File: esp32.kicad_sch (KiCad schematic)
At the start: 37 parts, among them J1 104426-8, J2 104426-8, SW1 SW_Push, SW2 SW_Push, SW3 SW_Push, SW4 SW_Push, U5 ESP32-WROOM-32D

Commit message: Organização do sheet esp32
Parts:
- renumbered C29 to C28, C30 to C29, C28 to C30
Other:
- moved on the sheet: C28, C29, J1, J2, R37, R38, R39, R40, R41, R42, R43, R44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

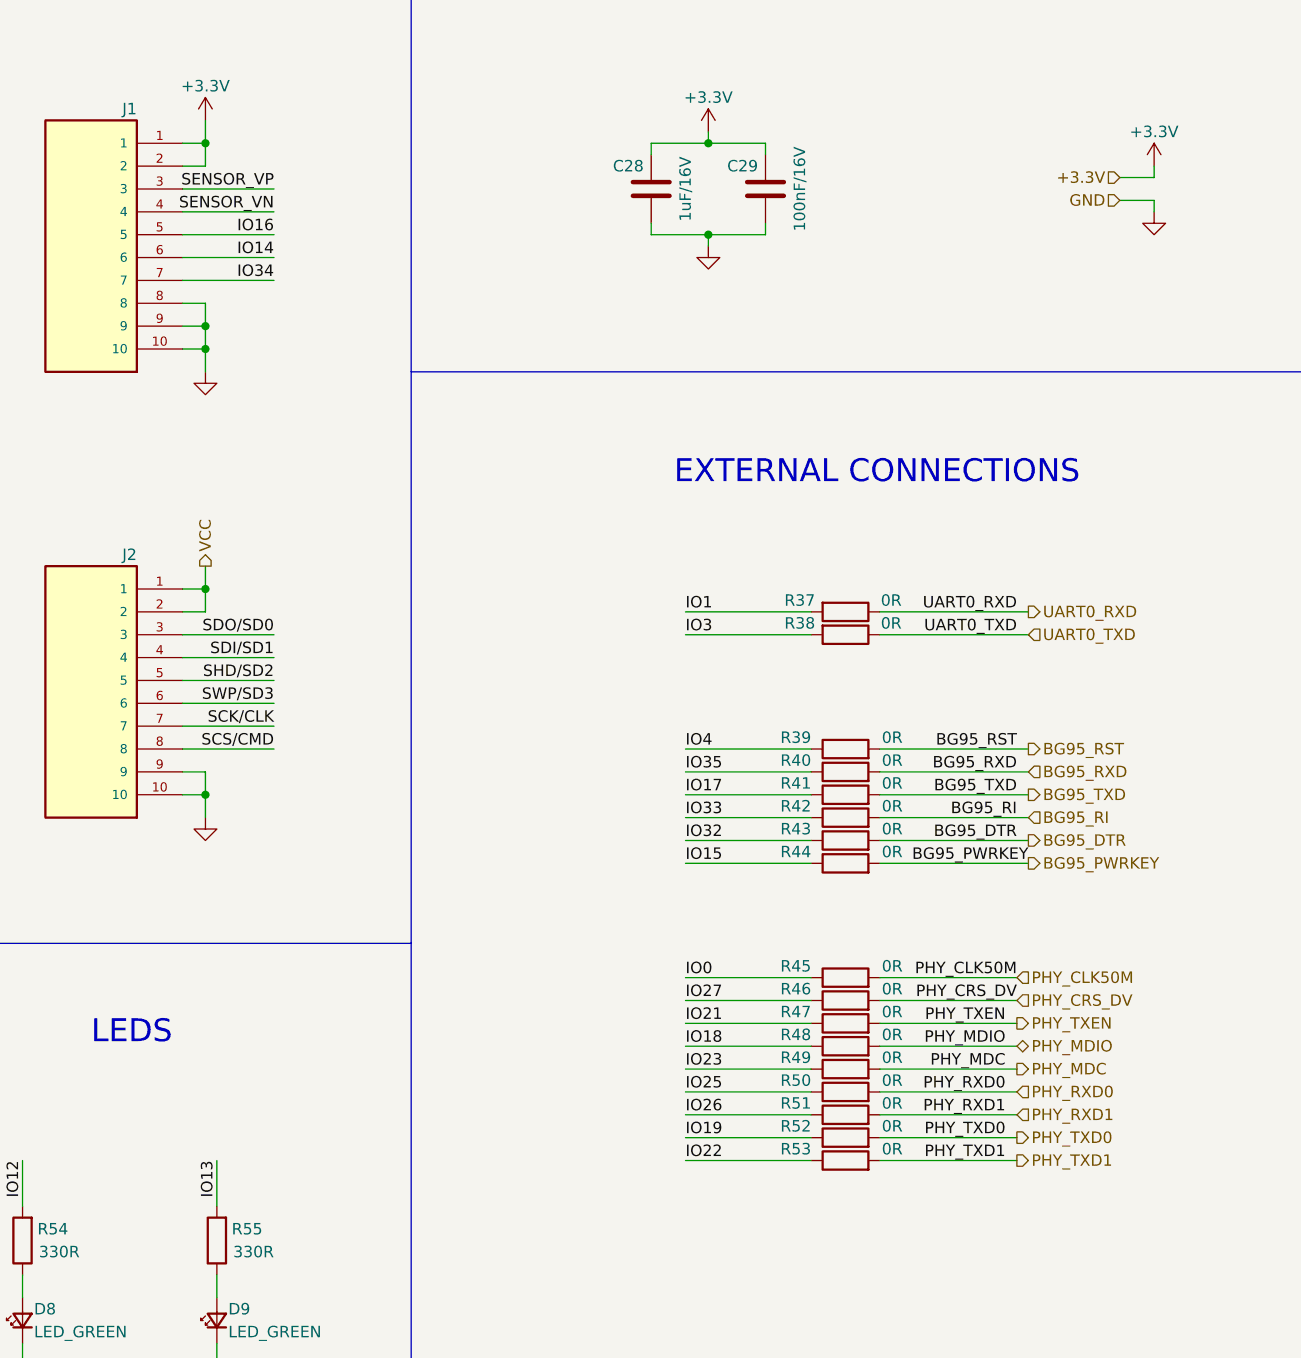
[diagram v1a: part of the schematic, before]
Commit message: Inserido um pino de controle de reset do PHY
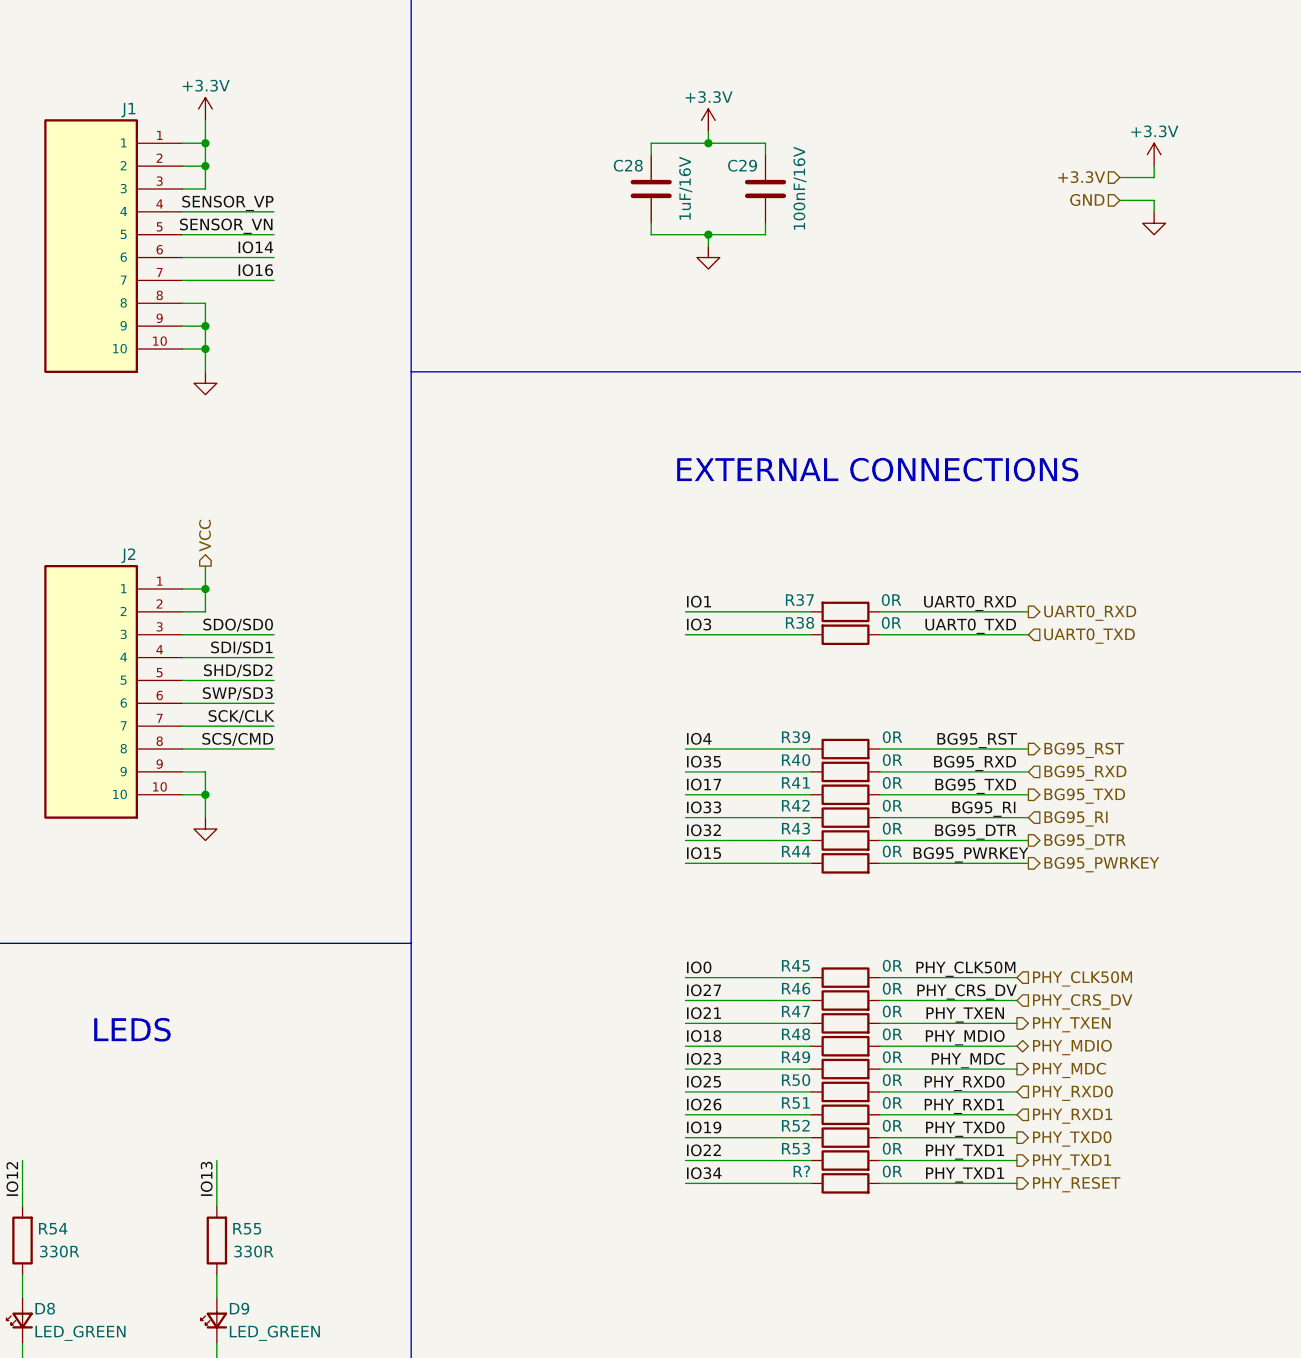
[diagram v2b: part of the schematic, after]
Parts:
- added R?: 0R, Resistor_SMD:R_0603_1608Metric_Pad0.98x0.95mm_HandSolder, symbol Device:R
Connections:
- net +3V3: now also J1.3
- net IO16: now also J1.7; no longer J1.5
- net IO34: now also R?.1; no longer J1.7
- net SENSOR_VN: now also J1.5; no longer J1.4
- net SENSOR_VP: now also J1.4; no longer J1.3
- net PHY_TXD1 renamed PHY_RESET
- net PHY_RESET: now also R?.2
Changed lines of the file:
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@@
   (junction (at 153.67 111.76) (diameter 0) (color 0 0 0 0)
   )
+  (junction (at 153.67 41.91) (diameter 0) (color 0 0 0 0)
+  )
   (junction (at 209.55 39.37) (diameter 0) (color 0 0 0 0)
   )
@@
     (stroke (width 0) (type default) (color 0 0 0 0))
   )
+  (wire (pts (xy 151.13 54.61) (xy 161.29 54.61))
+    (stroke (width 0) (type default) (color 0 0 0 0))
+  )
   (wire (pts (xy 220.98 91.44) (xy 207.01 91.44))
     (stroke (width 0) (type default) (color 0 0 0 0))
@@
     (stroke (width 0) (type default) (color 0 0 0 0))
   )
+  (wire (pts (xy 207.01 154.94) (xy 220.98 154.94))
+    (stroke (width 0) (type default) (color 0 0 0 0))
+  )
   (wire (pts (xy 228.6 137.16) (xy 243.84 137.16))
     (stroke (width 0) (type default) (color 0 0 0 0))
@@
     (stroke (width 0) (type default) (color 0 0 0 0))
   )
+  (wire (pts (xy 228.6 154.94) (xy 243.84 154.94))
+    (stroke (width 0) (type default) (color 0 0 0 0))
+  )
   (wire (pts (xy 90.17 96.52) (xy 99.06 96.52))
     (stroke (width 0) (type default) (color 0 0 0 0))
@@
     (stroke (width 0) (type default) (color 0 0 0 0))
   )
+  (wire (pts (xy 153.67 44.45) (xy 153.67 41.91))
+    (stroke (width 0) (type default) (color 0 0 0 0))
+  )
   (wire (pts (xy 228.6 111.76) (xy 245.11 111.76))
     (stroke (width 0) (type default) (color 0 0 0 0))
@@
     (stroke (width 0) (type default) (color 0 0 0 0))
   )
-  (wire (pts (xy 151.13 54.61) (xy 161.29 54.61))
-    (stroke (width 0) (type default) (color 0 0 0 0))
-  )
   (wire (pts (xy 215.9 48.26) (xy 215.9 49.53))
     (stroke (width 0) (type default) (color 0 0 0 0))
@@
     (stroke (width 0) (type default) (color 0 0 0 0))
   )
-  (wire (pts (xy 151.13 44.45) (xy 161.29 44.45))
-    (stroke (width 0) (type default) (color 0 0 0 0))
-  )
   (wire (pts (xy 153.67 36.83) (xy 153.67 39.37))
     (stroke (width 0) (type default) (color 0 0 0 0))
@@
   )
   (wire (pts (xy 228.6 91.44) (xy 245.11 91.44))
+    (stroke (width 0) (type default) (color 0 0 0 0))
+  )
+  (wire (pts (xy 151.13 44.45) (xy 153.67 44.45))
     (stroke (width 0) (type default) (color 0 0 0 0))
   )
@@
     (effects (font (size 1.27 1.27)) (justify left bottom))
   )
-  (label "IO16" (at 161.29 49.53 180)
+  (label "SENSOR_VN" (at 161.29 49.53 180)
     (effects (font (size 1.27 1.27)) (justify right bottom))
   )
@@
     (effects (font (size 1.27 1.27)) (justify left bottom))
   )
+  (label "PHY_TXD1" (at 242.57 154.94 180)
+    (effects (font (size 1.27 1.27)) (justify right bottom))
+  )
   (label "PHY_TXD0" (at 242.57 149.86 180)
     (effects (font (size 1.27 1.27)) (justify right bottom))
@@
     (effects (font (size 1.27 1.27)) (justify left bottom))
   )
-  (label "SENSOR_VN" (at 161.29 46.99 180)
+  (label "SENSOR_VP" (at 161.29 46.99 180)
     (effects (font (size 1.27 1.27)) (justify right bottom))
   )
@@
     (effects (font (size 1.27 1.27)) (justify right bottom))
   )
-  (label "IO34" (at 161.29 54.61 180)
-    (effects (font (size 1.27 1.27)) (justify right bottom))
+  (label "IO34" (at 207.01 154.94 0)
+    (effects (font (size 1.27 1.27)) (justify left bottom))
   )
   (label "IO32" (at 207.01 116.84 0)
@@
     (effects (font (size 1.27 1.27)) (justify left bottom))
   )
-  (label "SENSOR_VP" (at 161.29 44.45 180)
-    (effects (font (size 1.27 1.27)) (justify right bottom))
-  )
   (label "SENSOR_VP" (at 48.26 50.8 0)
     (effects (font (size 1.27 1.27)) (justify left bottom))
@@
   )
   (label "IO1" (at 99.06 48.26 180)
+    (effects (font (size 1.27 1.27)) (justify right bottom))
+  )
+  (label "IO16" (at 161.29 54.61 180)
     (effects (font (size 1.27 1.27)) (justify right bottom))
   )
@@
   )
   (hierarchical_label "PHY_CRS_DV" (shape input) (at 243.84 134.62 0)
+    (effects (font (size 1.27 1.27)) (justify left))
+  )
+  (hierarchical_label "PHY_RESET" (shape output) (at 243.84 154.94 0)
     (effects (font (size 1.27 1.27)) (justify left))
   )
@@
     (pin "9")
   )
+  (symbol (lib_id "Device:R") (at 224.79 154.94 90) (unit 1)
+    (in_bom yes) (on_board yes)
+    (property "Reference" "R?" (id 0) (at 220.98 153.67 90)
+      (effects (font (size 1.27 1.27)) (justify left))
+    )
+    (property "Value" "0R" (id 1) (at 231.14 153.67 90)
+      (effects (font (size 1.27 1.27)) (justify left))
+    )
+    (property "Footprint" "Resistor_SMD:R_0603_1608Metric_Pad0.98x0.95mm_HandSolder" (id 2) (at 224.79 156.718 90)
+      (effects (font (size 1.27 1.27)) hide)
+    )
+    (property "Datasheet" "~" (id 3) (at 224.79 154.94 0)
+      (effects (font (size 1.27 1.27)) hide)
+    )
+    (pin "1")
+    (pin "2")
+  )
   (symbol (lib_id "Device:R") (at 224.79 132.08 90) (unit 1)

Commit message: Referencia dos componentes
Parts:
- gave numbers to parts that had none: 1
- renumbered R36 to R37, R37 to R38, R38 to R39, R39 to R40, R40 to R41, R41 to R42, R42 to R43, R43 to R44, R44 to R45, R45 to R46, R46 to R47, R47 to R48, R48 to R49, R49 to R50, R50 to R51, R51 to R52, R52 to R53, R53 to R54, R54 to R56, R55 to R57, R56 to R58, R57 to R59

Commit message: Capacitores com encapsulamento 0603
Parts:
- C28: value 1uF/16V -> (none); footprint Capacitor_SMD:C_0603_1608Metric_Pad1.08x0.95mm_HandSolder -> (none)
- C29, C30, C31, C32, C33: value 100nF/16V -> (none); footprint Capacitor_SMD:C_0402_1005Metric_Pad0.74x0.62mm_HandSolder -> (none)
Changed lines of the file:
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@@
     (in_bom yes) (on_board yes)
     (property "Reference" "C28" (id 0) (at 200.66 41.91 0))
-    (property "Value" "1uF/16V" (id 1) (at 207.01 44.45 90))
-    (property "Footprint" "Capacitor_SMD:C_0603_1608Metric_Pad1.08x0.95mm_HandSolder" (id 2) (at 202.2348 40.64 0)
+    (property "Value" "" (id 1) (at 207.01 44.45 90))
+    (property "Footprint" "" (id 2) (at 202.2348 40.64 0)
       (effects (font (size 1.27 1.27)) hide)
     )
@@
     (in_bom yes) (on_board yes)
     (property "Reference" "C32" (id 0) (at 73.66 171.45 90))
-    (property "Value" "100nF/16V" (id 1) (at 73.66 179.07 90))
-    (property "Footprint" "Capacitor_SMD:C_0402_1005Metric_Pad0.74x0.62mm_HandSolder" (id 2) (at 69.85 176.2252 0)
+    (property "Value" "" (id 1) (at 73.66 179.07 90))
+    (property "Footprint" "" (id 2) (at 69.85 176.2252 0)
       (effects (font (size 1.27 1.27)) hide)
     )
@@
     (in_bom yes) (on_board yes)
     (property "Reference" "C31" (id 0) (at 45.72 171.45 90))
-    (property "Value" "100nF/16V" (id 1) (at 45.72 179.07 90))
-    (property "Footprint" "Capacitor_SMD:C_0402_1005Metric_Pad0.74x0.62mm_HandSolder" (id 2) (at 41.91 176.2252 0)
+    (property "Value" "" (id 1) (at 45.72 179.07 90))
+    (property "Footprint" "" (id 2) (at 41.91 176.2252 0)
       (effects (font (size 1.27 1.27)) hide)
     )
@@
     (in_bom yes) (on_board yes)
     (property "Reference" "C29" (id 0) (at 213.36 41.91 0))
-    (property "Value" "100nF/16V" (id 1) (at 219.71 44.45 90))
-    (property "Footprint" "Capacitor_SMD:C_0402_1005Metric_Pad0.74x0.62mm_HandSolder" (id 2) (at 214.9348 40.64 0)
+    (property "Value" "" (id 1) (at 219.71 44.45 90))
+    (property "Footprint" "" (id 2) (at 214.9348 40.64 0)
       (effects (font (size 1.27 1.27)) hide)
     )
@@
     (in_bom yes) (on_board yes)
     (property "Reference" "C33" (id 0) (at 101.6 171.45 90))
-    (property "Value" "100nF/16V" (id 1) (at 101.6 179.07 90))
-    (property "Footprint" "Capacitor_SMD:C_0402_1005Metric_Pad0.74x0.62mm_HandSolder" (id 2) (at 97.79 176.2252 0)
+    (property "Value" "" (id 1) (at 101.6 179.07 90))
+    (property "Footprint" "" (id 2) (at 97.79 176.2252 0)
       (effects (font (size 1.27 1.27)) hide)
     )
@@
     (in_bom yes) (on_board yes)
     (property "Reference" "C30" (id 0) (at 38.4551 48.5962 0))
-    (property "Value" "100nF/16V" (id 1) (at 44.3458 51.6899 90))
-    (property "Footprint" "Capacitor_SMD:C_0402_1005Metric_Pad0.74x0.62mm_HandSolder" (id 2) (at 39.6748 46.99 0)
-      (effects (font (size 1.27 1.27)) hide)
-    )
+    (property "Value" "" (id 1) (at 44.3458 51.6899 90))
+    (property "Footprint" "" (id 2) (at 39.6748 46.99 0)
+      (effects (font (size 1.27 1.27)) hide)
+    )

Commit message: Adicionado os pads dos Test Point e alterado o Bead
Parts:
- C28: value (none) -> 1uF/16V; footprint (none) -> Capacitor_SMD:C_0603_1608Metric_Pad1.08x0.95mm_HandSolder
- C29, C30, C31, C32, C33: value (none) -> 100nF/16V; footprint (none) -> Capacitor_SMD:C_0603_1608Metric_Pad1.08x0.95mm_HandSolder
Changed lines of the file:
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@@
     (in_bom yes) (on_board yes)
     (property "Reference" "C28" (id 0) (at 200.66 41.91 0))
-    (property "Value" "" (id 1) (at 207.01 44.45 90))
-    (property "Footprint" "" (id 2) (at 202.2348 40.64 0)
+    (property "Value" "1uF/16V" (id 1) (at 207.01 44.45 90))
+    (property "Footprint" "Capacitor_SMD:C_0603_1608Metric_Pad1.08x0.95mm_HandSolder" (id 2) (at 202.2348 40.64 0)
       (effects (font (size 1.27 1.27)) hide)
     )
@@
     (in_bom yes) (on_board yes)
     (property "Reference" "C32" (id 0) (at 73.66 171.45 90))
-    (property "Value" "" (id 1) (at 73.66 179.07 90))
-    (property "Footprint" "" (id 2) (at 69.85 176.2252 0)
+    (property "Value" "100nF/16V" (id 1) (at 73.66 179.07 90))
+    (property "Footprint" "Capacitor_SMD:C_0603_1608Metric_Pad1.08x0.95mm_HandSolder" (id 2) (at 69.85 176.2252 0)
       (effects (font (size 1.27 1.27)) hide)
     )
@@
     (in_bom yes) (on_board yes)
     (property "Reference" "C31" (id 0) (at 45.72 171.45 90))
-    (property "Value" "" (id 1) (at 45.72 179.07 90))
-    (property "Footprint" "" (id 2) (at 41.91 176.2252 0)
+    (property "Value" "100nF/16V" (id 1) (at 45.72 179.07 90))
+    (property "Footprint" "Capacitor_SMD:C_0603_1608Metric_Pad1.08x0.95mm_HandSolder" (id 2) (at 41.91 176.2252 0)
       (effects (font (size 1.27 1.27)) hide)
     )
@@
     (in_bom yes) (on_board yes)
     (property "Reference" "C29" (id 0) (at 213.36 41.91 0))
-    (property "Value" "" (id 1) (at 219.71 44.45 90))
-    (property "Footprint" "" (id 2) (at 214.9348 40.64 0)
+    (property "Value" "100nF/16V" (id 1) (at 219.71 44.45 90))
+    (property "Footprint" "Capacitor_SMD:C_0603_1608Metric_Pad1.08x0.95mm_HandSolder" (id 2) (at 214.9348 40.64 0)
       (effects (font (size 1.27 1.27)) hide)
     )
@@
     (in_bom yes) (on_board yes)
     (property "Reference" "C33" (id 0) (at 101.6 171.45 90))
-    (property "Value" "" (id 1) (at 101.6 179.07 90))
-    (property "Footprint" "" (id 2) (at 97.79 176.2252 0)
+    (property "Value" "100nF/16V" (id 1) (at 101.6 179.07 90))
+    (property "Footprint" "Capacitor_SMD:C_0603_1608Metric_Pad1.08x0.95mm_HandSolder" (id 2) (at 97.79 176.2252 0)
       (effects (font (size 1.27 1.27)) hide)
     )
@@
     (in_bom yes) (on_board yes)
     (property "Reference" "C30" (id 0) (at 38.4551 48.5962 0))
-    (property "Value" "" (id 1) (at 44.3458 51.6899 90))
-    (property "Footprint" "" (id 2) (at 39.6748 46.99 0)
-      (effects (font (size 1.27 1.27)) hide)
-    )
+    (property "Value" "100nF/16V" (id 1) (at 44.3458 51.6899 90))
+    (property "Footprint" "Capacitor_SMD:C_0603_1608Metric_Pad1.08x0.95mm_HandSolder" (id 2) (at 39.6748 46.99 0)
+      (effects (font (size 1.27 1.27)) hide)
+    )
